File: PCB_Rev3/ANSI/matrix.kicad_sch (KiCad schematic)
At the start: 124 parts

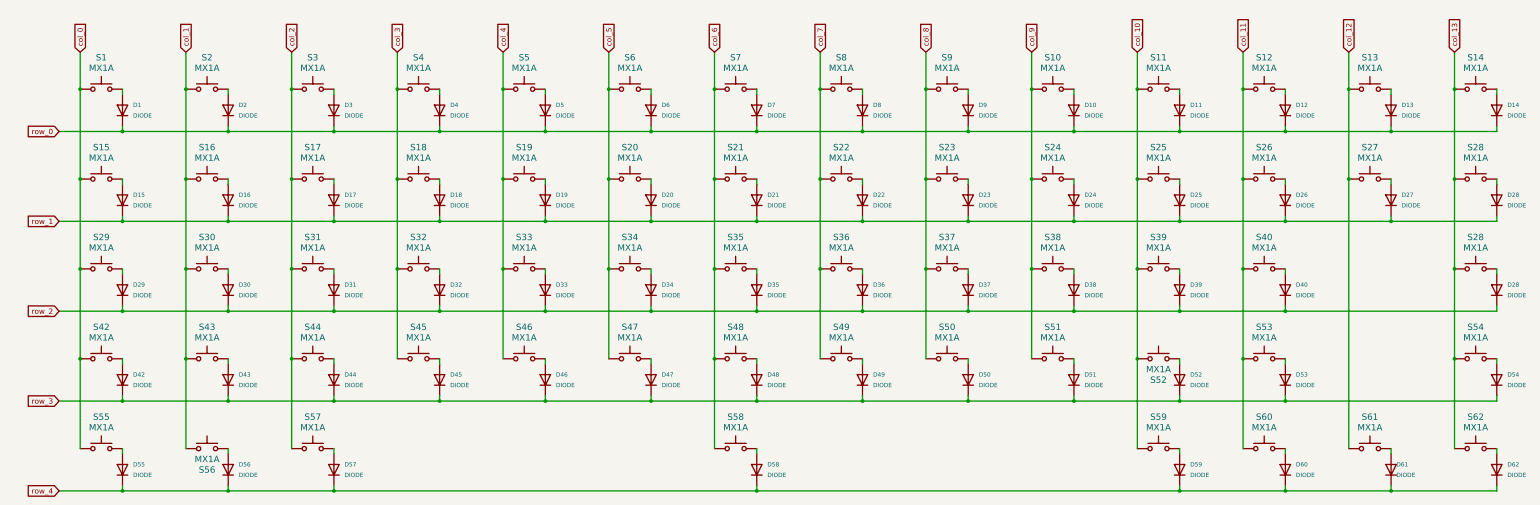
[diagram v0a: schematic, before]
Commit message: Better wiring.
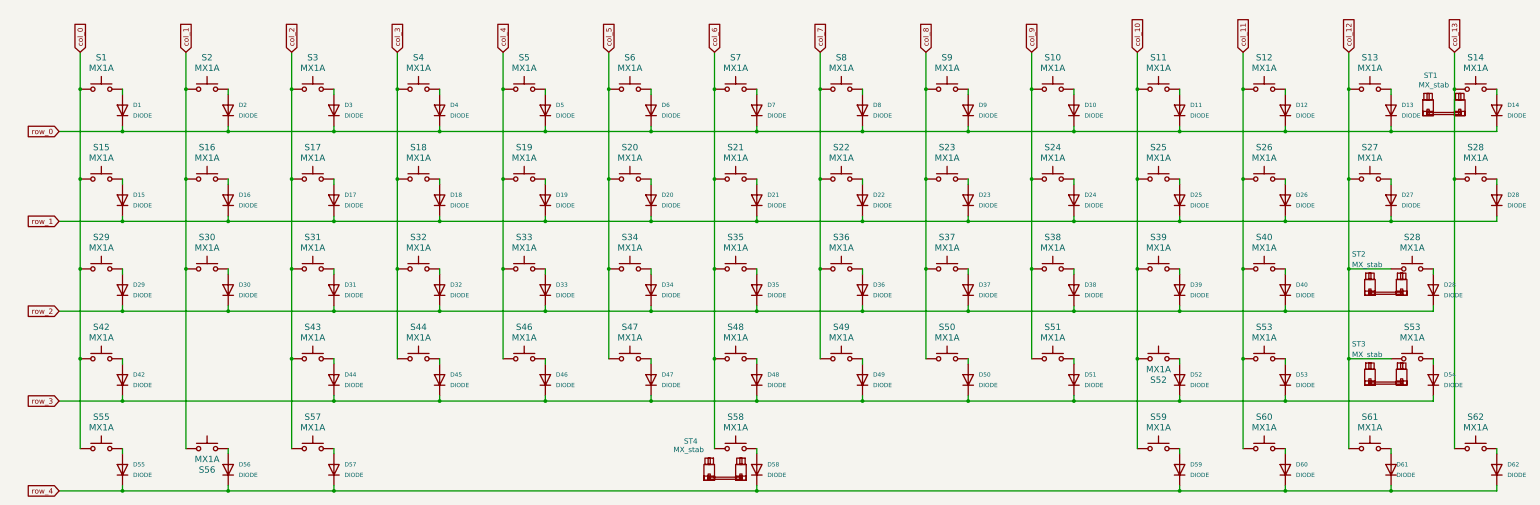
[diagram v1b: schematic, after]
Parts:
- removed D43: DIODE, Diode_SMD:D_SOD-323_HandSoldering, symbol Device:D
- removed S43: MX1A, PCM_Switch_Keyboard_Hotswap_Kailh:SW_Hotswap_Kailh_MX_Plated_1.00u, symbol Switch:SW_Push
- added ST1, ST2, ST3: MX_stab, PCM_Mounting_Keyboard_Stabilizer:Stabilizer_Cherry_MX_2.00u, symbol PCM_marbastlib-mx:MX_stab
- added ST4: MX_stab, PCM_Mounting_Keyboard_Stabilizer:Stabilizer_Cherry_MX_6.25u, symbol PCM_marbastlib-mx:MX_stab
- S42: footprint PCM_Switch_Keyboard_Hotswap_Kailh:SW_Hotswap_Kailh_MX_Plated_1.25u -> PCM_Switch_Keyboard_Hotswap_Kailh:SW_Hotswap_Kailh_MX_Plated_2.25u
- renumbered S44 to S43, S45 to S44, S54 to S53
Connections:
- net col_12: now also S28.2, S53.2
- net col_13: no longer S28.2, S53.2
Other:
- moved on the sheet: D28, D54, S28, S53

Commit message: Add wireless part
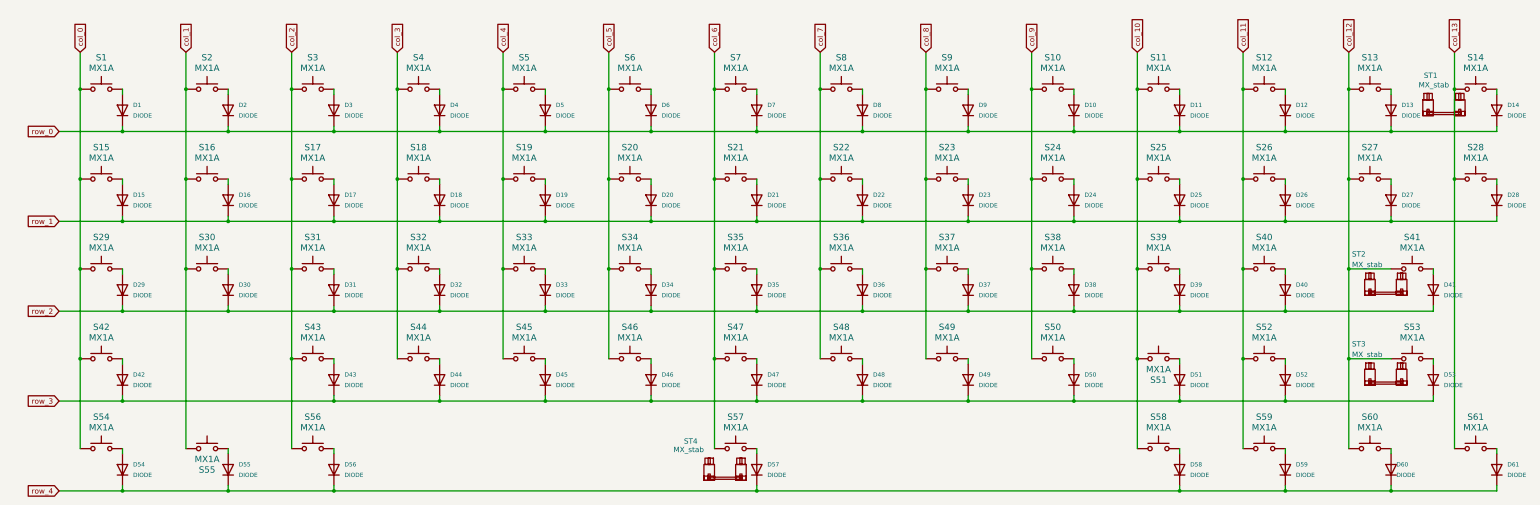
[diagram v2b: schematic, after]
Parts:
- renumbered D28 to D41, D44 to D43, D45 to D44, D46 to D45, D47 to D46, D48 to D47, D49 to D48, D50 to D49, D51 to D50, D52 to D51, D53 to D52, D54 to D53, D55 to D54, D56 to D55, D57 to D56, D58 to D57, D59 to D58, D60 to D59, D61 to D60, D62 to D61, S28 to S41, S46 to S45, S47 to S46, S48 to S47, S49 to S48, S50 to S49, S51 to S50, S52 to S51, S53 to S52, S55 to S54, S56 to S55, S57 to S56, S58 to S57, S59 to S58, S60 to S59, S61 to S60, S62 to S61
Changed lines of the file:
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@@
 (kicad_sch
-	(version 20231120)
+	(version 20250114)
 	(generator "eeschema")
-	(generator_version "8.0")
+	(generator_version "9.0")
 	(paper "A3")
 	(junction
@@
 		(dnp no)
 		(fields_autoplaced yes)
-		(property "Reference" "D62"
+		(property "Reference" "D61"
 			(at 386.08 151.1299 90)
 			(effects
@@
 		(dnp no)
 		(fields_autoplaced yes)
-		(property "Reference" "S46"
+		(property "Reference" "S45"
 			(at 149.86 118.11 0)
 			(effects
@@
 		(dnp no)
 		(fields_autoplaced yes)
-		(property "Reference" "D56"
+		(property "Reference" "D55"
 			(at 81.28 151.1299 90)
 			(effects
@@
 		(dnp no)
 		(fields_autoplaced yes)
-		(property "Reference" "D60"
+		(property "Reference" "D59"
 			(at 335.28 151.1299 90)
 			(effects
@@
 		(dnp no)
 		(fields_autoplaced yes)
-		(property "Reference" "D58"
+		(property "Reference" "D57"
 			(at 208.28 151.1299 90)
 			(effects
@@
 		(dnp no)
 		(fields_autoplaced yes)
-		(property "Reference" "D51"
+		(property "Reference" "D50"
 			(at 284.48 129.5399 90)
 			(effects
@@
 		(dnp no)
 		(fields_autoplaced yes)
-		(property "Reference" "D44"
+		(property "Reference" "D43"
 			(at 106.68 129.5399 90)
 			(effects
@@
 		(dnp no)
 		(fields_autoplaced yes)
-		(property "Reference" "D28"
+		(property "Reference" "D41"
 			(at 370.84 107.9499 90)
 			(effects
@@
 		(dnp no)
 		(fields_autoplaced yes)
-		(property "Reference" "D47"
+		(property "Reference" "D46"
 			(at 182.88 129.5399 90)
 			(effects
@@
 		(dnp no)
 		(fields_autoplaced yes)
-		(property "Reference" "D45"
+		(property "Reference" "D44"
 			(at 132.08 129.5399 90)
 			(effects
@@
 		(dnp no)
 		(fields_autoplaced yes)
-		(property "Reference" "S58"
+		(property "Reference" "S57"
 			(at 200.66 139.7 0)
 			(effects
@@
 		(dnp no)
 		(fields_autoplaced yes)
-		(property "Reference" "S57"
+		(property "Reference" "S56"
 			(at 99.06 139.7 0)
 			(effects
@@
 		(on_board yes)
 		(dnp no)
-		(property "Reference" "D61"
+		(property "Reference" "D60"
 			(at 359.41 151.1299 90)
 			(effects
@@
 		(dnp no)
 		(fields_autoplaced yes)
-		(property "Reference" "S61"
+		(property "Reference" "S60"
 			(at 353.06 139.7 0)
 			(effects
@@
 		(dnp no)
 		(fields_autoplaced yes)
-		(property "Reference" "D49"
+		(property "Reference" "D48"
 			(at 233.68 129.5399 90)
 			(effects
@@
 		(dnp no)
 		(fields_autoplaced yes)
-		(property "Reference" "S51"
+		(property "Reference" "S50"
 			(at 276.86 118.11 0)
 			(effects
@@
 		(dnp no)
 		(fields_autoplaced yes)
-		(property "Reference" "D52"
+		(property "Reference" "D51"
 			(at 309.88 129.5399 90)
 			(effects
@@
 		(dnp no)
 		(fields_autoplaced yes)
-		(property "Reference" "D50"
+		(property "Reference" "D49"
 			(at 259.08 129.5399 90)
 			(effects
@@
 		(dnp no)
 		(fields_autoplaced yes)
-		(property "Reference" "S50"
+		(property "Reference" "S49"
 			(at 251.46 118.11 0)
 			(effects
@@
 		(dnp no)
 		(fields_autoplaced yes)
-		(property "Reference" "D59"
+		(property "Reference" "D58"
 			(at 309.88 151.1299 90)
 			(effects
@@
 		(dnp no)
 		(fields_autoplaced yes)
-		(property "Reference" "S59"
+		(property "Reference" "S58"
 			(at 302.26 139.7 0)
 			(effects
@@
 		(dnp no)
 		(fields_autoplaced yes)
-		(property "Reference" "S48"
+		(property "Reference" "S47"
 			(at 200.66 118.11 0)
 			(effects
@@
 		(dnp no)
 		(fields_autoplaced yes)
-		(property "Reference" "S53"
+		(property "Reference" "S52"
 			(at 327.66 118.11 0)
 			(effects
@@
 		(on_board yes)
 		(dnp no)
-		(property "Reference" "S56"
+		(property "Reference" "S55"
 			(at 73.66 152.4 0)
 			(effects
@@
 		(dnp no)
 		(fields_autoplaced yes)
-		(property "Reference" "S55"
+		(property "Reference" "S54"
 			(at 48.26 139.7 0)
 			(effects
@@
 		(on_board yes)
 		(dnp no)
-		(property "Reference" "S52"
+		(property "Reference" "S51"
 			(at 302.26 130.81 0)
 			(effects
@@
 		(dnp no)
 		(fields_autoplaced yes)
-		(property "Reference" "S62"
+		(property "Reference" "S61"
 			(at 378.46 139.7 0)
 			(effects
@@
 		(dnp no)
 		(fields_autoplaced yes)
-		(property "Reference" "D53"
+		(property "Reference" "D52"
 			(at 335.28 129.5399 90)
 			(effects
@@
 		(dnp no)
 		(fields_autoplaced yes)
-		(property "Reference" "D55"
+		(property "Reference" "D54"
 			(at 55.88 151.1299 90)
 			(effects
@@
 		(dnp no)
 		(fields_autoplaced yes)
-		(property "Reference" "S28"
+		(property "Reference" "S41"
 			(at 363.22 96.52 0)
 			(effects
@@
 		(dnp no)
 		(fields_autoplaced yes)
-		(property "Reference" "D46"
+		(property "Reference" "D45"
 			(at 157.48 129.5399 90)
 			(effects
@@
 		(dnp no)
 		(fields_autoplaced yes)
-		(property "Reference" "S60"
+		(property "Reference" "S59"
 			(at 327.66 139.7 0)
 			(effects
@@
 		(dnp no)
 		(fields_autoplaced yes)
-		(property "Reference" "D48"
+		(property "Reference" "D47"
 			(at 208.28 129.5399 90)
 			(effects
@@
 		(dnp no)
 		(fields_autoplaced yes)
-		(property "Reference" "D57"
+		(property "Reference" "D56"
 			(at 106.68 151.1299 90)
 			(effects
@@
 		(dnp no)
 		(fields_autoplaced yes)
-		(property "Reference" "D54"
+		(property "Reference" "D53"
 			(at 370.84 129.5399 90)
 			(effects
@@
 		(dnp no)
 		(fields_autoplaced yes)
-		(property "Reference" "S49"
+		(property "Reference" "S48"
 			(at 226.06 118.11 0)
 			(effects
@@
 		(dnp no)
 		(fields_autoplaced yes)
-		(property "Reference" "S47"
+		(property "Reference" "S46"
 			(at 175.26 118.11 0)
 			(effects

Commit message: Finish board design
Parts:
- renumbered D9 to D10, D10 to D11, D11 to D12, D12 to D13, D13 to D14, D14 to D15, D15 to D16, D16 to D17, D17 to D18, D18 to D19, D1 to D2, D19 to D20, D20 to D21, D21 to D22, D22 to D23, D23 to D24, D24 to D25, D25 to D26, D26 to D27, D27 to D28, D28 to D29, D2 to D3, D29 to D30, D30 to D31, D31 to D32, D32 to D33, D33 to D34, D34 to D35, D35 to D36, D36 to D37, D37 to D38, D38 to D39, D3 to D4, D39 to D40, D40 to D41, D41 to D42, D42 to D43, D43 to D44, D44 to D45, D45 to D46, D46 to D47, D47 to D48, D48 to D49, D4 to D5, D49 to D50, D50 to D51, D51 to D52, D52 to D53, D53 to D54, D54 to D55, D55 to D56, D56 to D57, D57 to D58, D58 to D59, D5 to D6, D59 to D60, D60 to D61, D61 to D62, D6 to D7, D7 to D8, D8 to D9

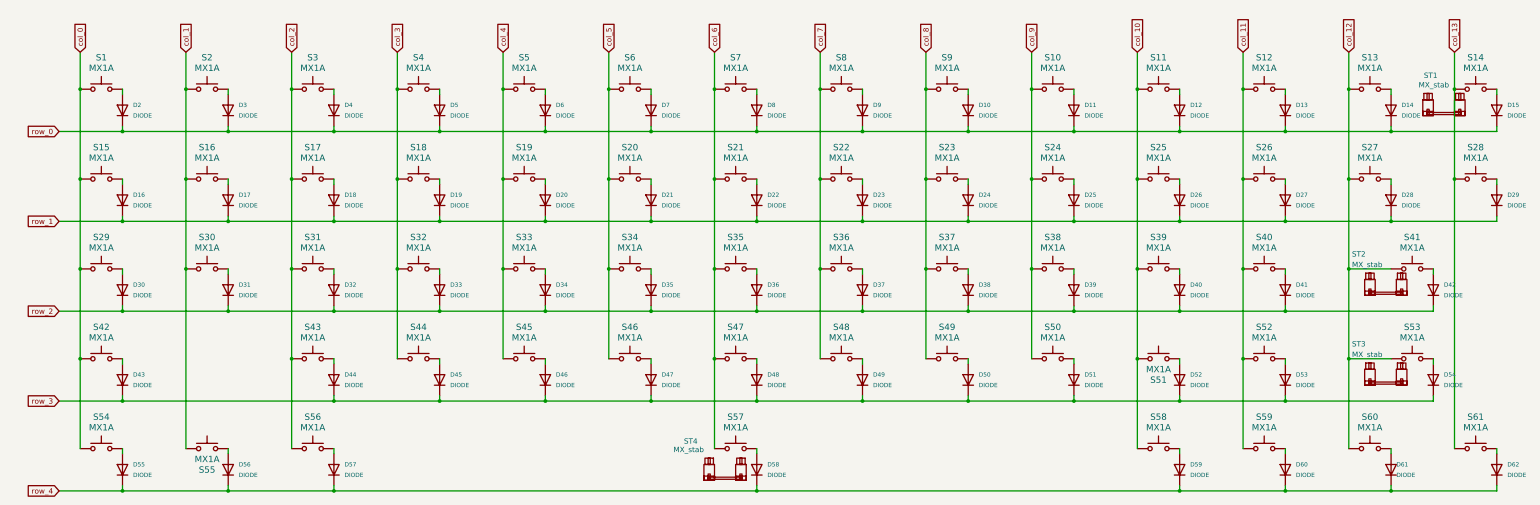
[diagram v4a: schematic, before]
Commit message: Add mounting hole
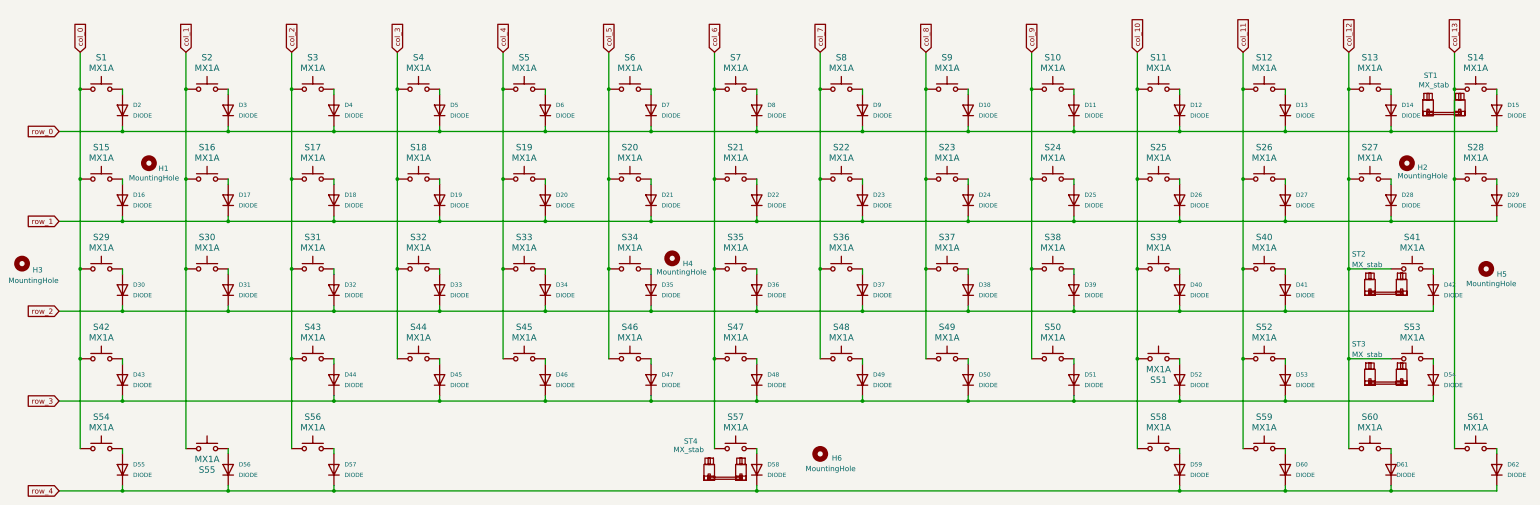
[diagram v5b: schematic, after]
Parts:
- added H1: MountingHole, PH60-hole:PKRHC, symbol Mechanical:MountingHole
- added H2, H6: MountingHole, PH60-hole:PKRH, symbol Mechanical:MountingHole
- added H3, H5: MountingHole, PH60-hole:PKRHSL, symbol Mechanical:MountingHole
- added H4: MountingHole, PH60-hole:PKRHHALF, symbol Mechanical:MountingHole

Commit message: REV3 与 REV3_A 合并
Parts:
- renumbered D9 to D10, D10 to D11, D11 to D12, D12 to D13, D13 to D14, D14 to D15, D15 to D16, D16 to D17, D17 to D18, D18 to D19, D19 to D20, D20 to D21, D21 to D22, D22 to D23, D23 to D24, D24 to D25, D25 to D26, D26 to D27, D27 to D28, D28 to D29, D2 to D3, D29 to D30, D30 to D31, D31 to D32, D32 to D33, D33 to D34, D34 to D35, D35 to D36, D36 to D37, D37 to D38, D38 to D39, D3 to D4, D39 to D40, D40 to D41, D41 to D42, D42 to D43, D43 to D44, D44 to D45, D45 to D46, D46 to D47, D47 to D48, D48 to D49, D4 to D5, D49 to D50, D50 to D51, D51 to D52, D52 to D53, D53 to D54, D54 to D55, D55 to D56, D56 to D57, D57 to D58, D58 to D59, D5 to D6, D59 to D60, D60 to D61, D61 to D62, D62 to D63, D6 to D7, D7 to D8, D8 to D9, H4 to H3, H3 to H4
